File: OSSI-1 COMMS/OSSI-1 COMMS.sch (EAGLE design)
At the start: 188 parts, among them Q1 NX-3215, U1 MAX2640, U10 MAX6369, U11 TPS3838, U12 MAX890L, U13 MCP1700_SOT23, U2 PE4259, U3 RF5110G, U4 OPA347, U5 MAX869L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

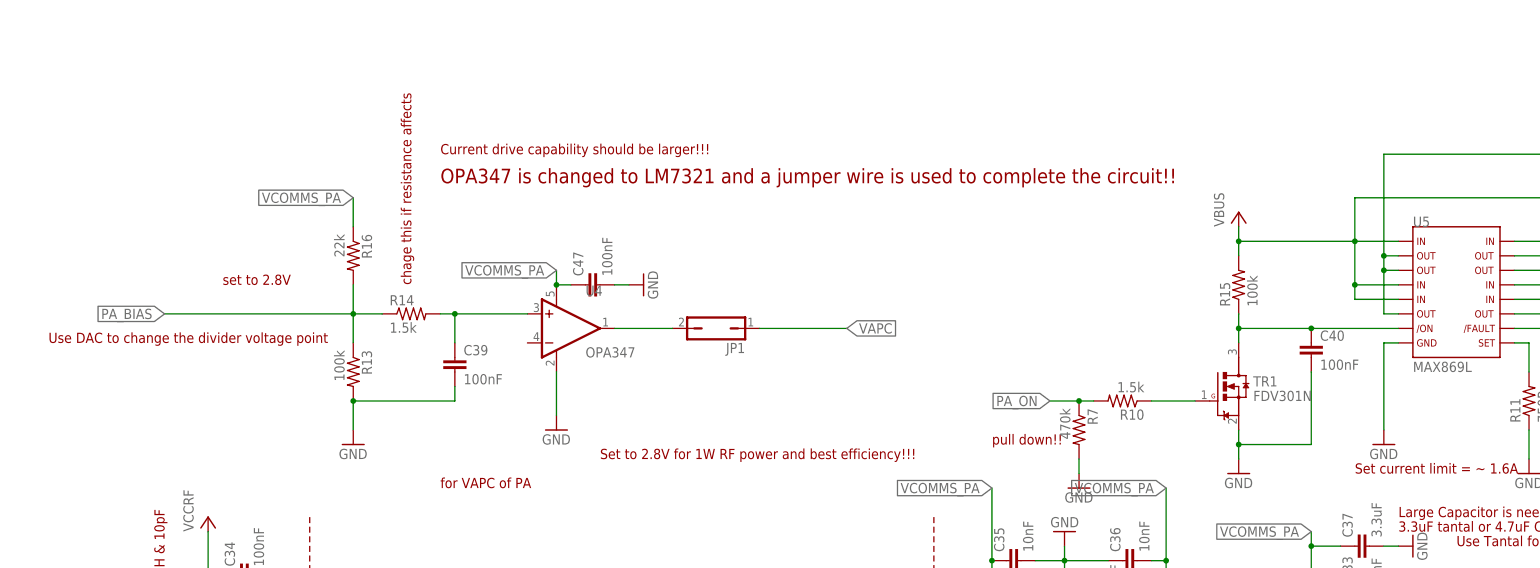
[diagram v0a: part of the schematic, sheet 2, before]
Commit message: opa347 setting corrected
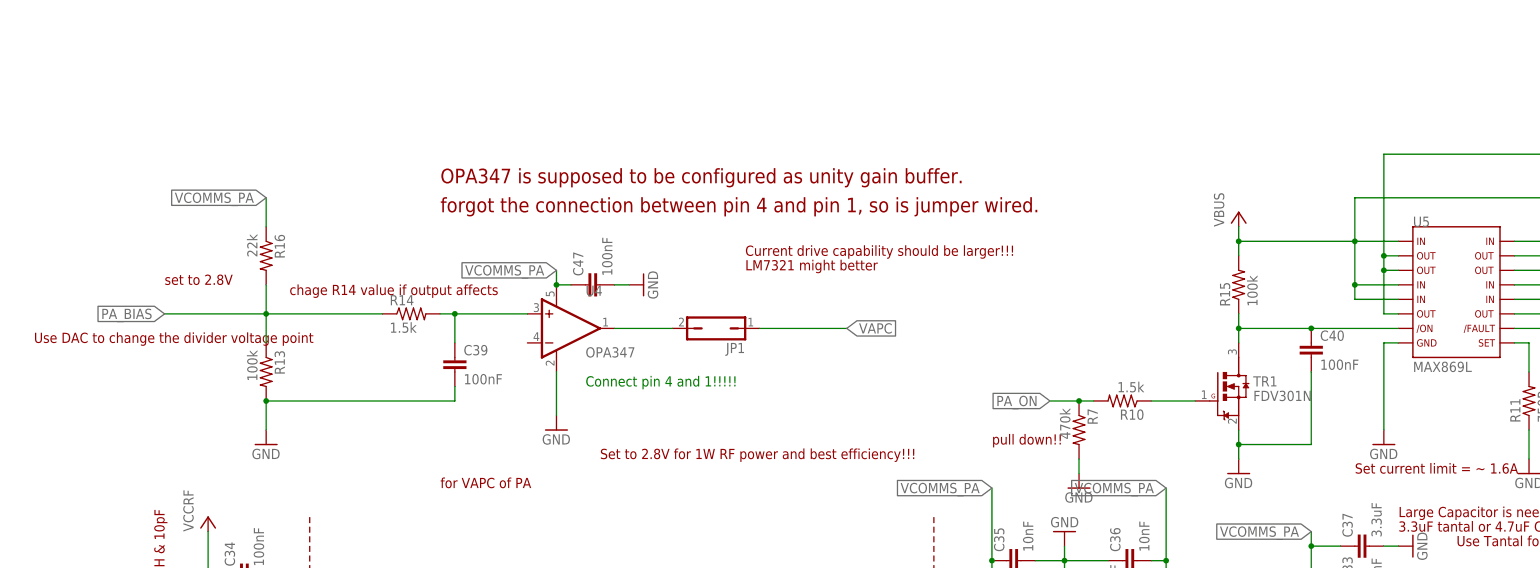
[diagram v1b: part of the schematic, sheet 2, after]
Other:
- note added: "Connect pin 4 and 1!!!!!"
- note added: "LM7321 might better"
- note added: "OPA347 is supposed to be configured as unity gain buffer."
- note added: "chage R14 value if output affects"
- note added: "forgot the connection between pin 4 and pin 1, so is jumper wired."
- note removed: "OPA347 is changed to LM7321 and a jumper wire is used to complete the circuit!!"
- note removed: "chage this if resistance affects"
- moved on the sheet: R13, R16
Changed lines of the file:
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@@
 <text x="269.24" y="55.88" size="1.778" layer="94">post impedance matching</text>
 <text x="78.74" y="200.66" size="1.778" layer="94">for VAPC of PA </text>
-<text x="40.64" y="236.22" size="1.778" layer="94">set to 2.8V</text>
-<text x="10.16" y="226.06" size="1.778" layer="94">Use DAC to change the divider voltage point</text>
+<text x="30.48" y="236.22" size="1.778" layer="94">set to 2.8V</text>
+<text x="7.62" y="226.06" size="1.778" layer="94">Use DAC to change the divider voltage point</text>
 <text x="27.94" y="147.32" size="1.778" layer="94">0dbm </text>
 <text x="292.1" y="162.56" size="1.778" layer="94">1Watt </text>
@@
 <text x="241.3" y="160.02" size="1.778" layer="94">important!!</text>
 <text x="233.68" y="165.1" size="1.778" layer="94">important!!</text>
-<text x="73.66" y="236.22" size="1.778" layer="94" rot="R90">chage this if resistance affects</text>
+<text x="88.9" y="236.22" size="1.778" layer="94" rot="R180">chage R14 value if output affects</text>
 <text x="175.26" y="208.28" size="1.778" layer="94">pull down!!</text>
 <wire x1="111.76" y1="91.44" x2="111.76" y2="25.4" width="0.1524" layer="94" style="shortdash"/>
@@
 <text x="30.48" y="160.02" size="1.778" layer="94" rot="R90">Eval board settng is 13nH &amp; 10pF</text>
 <text x="322.58" y="190.5" size="1.778" layer="94">Set VCOMMS_PA to 3.3~3.4V</text>
-<text x="78.74" y="259.08" size="1.778" layer="94">Current drive capability should be larger!!!</text>
-<text x="78.74" y="254" size="2.54" layer="94">OPA347 is changed to LM7321 and a jumper wire is used to complete the circuit!!</text>
+<text x="132.08" y="241.3" size="1.778" layer="94">Current drive capability should be larger!!!</text>
+<text x="78.74" y="254" size="2.54" layer="94">OPA347 is supposed to be configured as unity gain buffer.</text>
 <text x="106.68" y="205.74" size="1.778" layer="94">Set to 2.8V for 1W RF power and best efficiency!!!</text>
 <text x="200.66" y="93.98" size="1.778" layer="94">Use Tantal for larger RF out</text>
@@
 <text x="289.56" y="27.94" size="3.302" layer="94" font="vector">OPEN SOURSE SATELLITE INITIATIVE</text>
 <text x="289.56" y="25.4" size="2.54" layer="94" font="vector">http://opensat.cc</text>
+<text x="78.74" y="248.92" size="2.54" layer="94">forgot the connection between pin 4 and pin 1, so is jumper wired.</text>
+<text x="104.14" y="218.44" size="1.778" layer="91">Connect pin 4 and 1!!!!!</text>
+<text x="132.08" y="238.76" size="1.778" layer="94">LM7321 might better</text>
 </plain>
 <instances>
@@
 <instance part="VCCRF3" gate="G$1" x="38.1" y="195.58"/>
 <instance part="VCCRF4" gate="G$1" x="129.54" y="81.28"/>
-<instance part="R16" gate="G$1" x="63.5" y="241.3" rot="R270"/>
-<instance part="R13" gate="G$1" x="63.5" y="220.98" rot="R270"/>
+<instance part="R16" gate="G$1" x="48.26" y="241.3" rot="R270"/>
+<instance part="R13" gate="G$1" x="48.26" y="220.98" rot="R270"/>
 <instance part="C39" gate="G$1" x="81.28" y="223.52"/>
-<instance part="GND63" gate="1" x="63.5" y="208.28"/>
+<instance part="GND63" gate="1" x="48.26" y="208.28"/>
 <instance part="GND64" gate="1" x="99.06" y="210.82"/>
 <instance part="U4" gate="A" x="101.6" y="228.6"/>
@@
 <pinref part="GND63" gate="1" pin="GND"/>
 <pinref part="R13" gate="G$1" pin="2"/>
-<wire x1="63.5" y1="210.82" x2="63.5" y2="215.9" width="0.1524" layer="91"/>
+<wire x1="48.26" y1="210.82" x2="48.26" y2="215.9" width="0.1524" layer="91"/>
 <pinref part="C39" gate="G$1" pin="2"/>
 <wire x1="81.28" y1="218.44" x2="81.28" y2="215.9" width="0.1524" layer="91"/>
-<wire x1="81.28" y1="215.9" x2="63.5" y2="215.9" width="0.1524" layer="91"/>
-<junction x="63.5" y="215.9"/>
+<wire x1="81.28" y1="215.9" x2="48.26" y2="215.9" width="0.1524" layer="91"/>
+<junction x="48.26" y="215.9"/>
 </segment>
 <segment>
@@
 <segment>
 <pinref part="R16" gate="G$1" pin="1"/>
-<wire x1="63.5" y1="246.38" x2="63.5" y2="251.46" width="0.1524" layer="91"/>
-<label x="63.5" y="251.46" size="1.778" layer="95" rot="R180" xref="yes"/>
+<wire x1="48.26" y1="246.38" x2="48.26" y2="251.46" width="0.1524" layer="91"/>
+<label x="48.26" y="251.46" size="1.778" layer="95" rot="R180" xref="yes"/>
 </segment>
 <segment>
@@
 <segment>
 <pinref part="R16" gate="G$1" pin="2"/>
-<wire x1="63.5" y1="231.14" x2="63.5" y2="236.22" width="0.1524" layer="91"/>
+<wire x1="48.26" y1="231.14" x2="48.26" y2="236.22" width="0.1524" layer="91"/>
 <pinref part="R13" gate="G$1" pin="1"/>
-<wire x1="63.5" y1="231.14" x2="63.5" y2="226.06" width="0.1524" layer="91"/>
-<junction x="63.5" y="231.14"/>
-<wire x1="63.5" y1="231.14" x2="30.48" y2="231.14" width="0.1524" layer="91"/>
+<wire x1="48.26" y1="231.14" x2="48.26" y2="226.06" width="0.1524" layer="91"/>
+<junction x="48.26" y="231.14"/>
+<wire x1="48.26" y1="231.14" x2="30.48" y2="231.14" width="0.1524" layer="91"/>
 <label x="30.48" y="231.14" size="1.778" layer="95" rot="R180" xref="yes"/>
 <pinref part="R14" gate="G$1" pin="1"/>
-<wire x1="63.5" y1="231.14" x2="68.58" y2="231.14" width="0.1524" layer="91"/>
-</segment>
-</net>
+<wire x1="48.26" y1="231.14" x2="68.58" y2="231.14" width="0.1524" layer="91"/>
+</segment>
+</net>

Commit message: sch corrected
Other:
- note added: "15pF"
- note removed: "8.2nH"
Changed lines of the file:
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@@
 <text x="223.52" y="121.92" size="1.778" layer="94">10pF +6pF  is better than 16 pF why???</text>
 <text x="299.72" y="116.84" size="1.778" layer="94">tune RF switch to lower the insertion loss. currently around 1.2 dB loss!!!!</text>
-<text x="193.04" y="50.8" size="1.778" layer="91">1500pF</text>
-<text x="180.34" y="50.8" size="1.778" layer="91">47nH</text>
-<text x="116.84" y="45.72" size="1.778" layer="91">8.2nH</text>
+<text x="193.04" y="45.72" size="1.778" layer="91">1500pF</text>
+<text x="180.34" y="45.72" size="1.778" layer="91">47nH</text>
+<text x="116.84" y="45.72" size="1.778" layer="91">15pF</text>
 <text x="116.84" y="43.18" size="1.778" layer="91">Final Value but the result will be similar</text>
 <text x="48.26" y="66.04" size="1.778" layer="91">12pF</text>

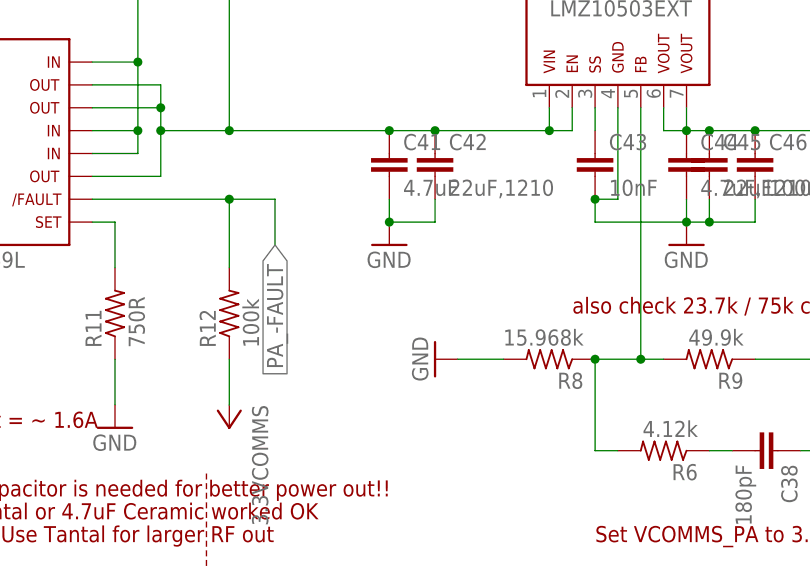
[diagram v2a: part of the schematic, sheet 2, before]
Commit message: value comment changed
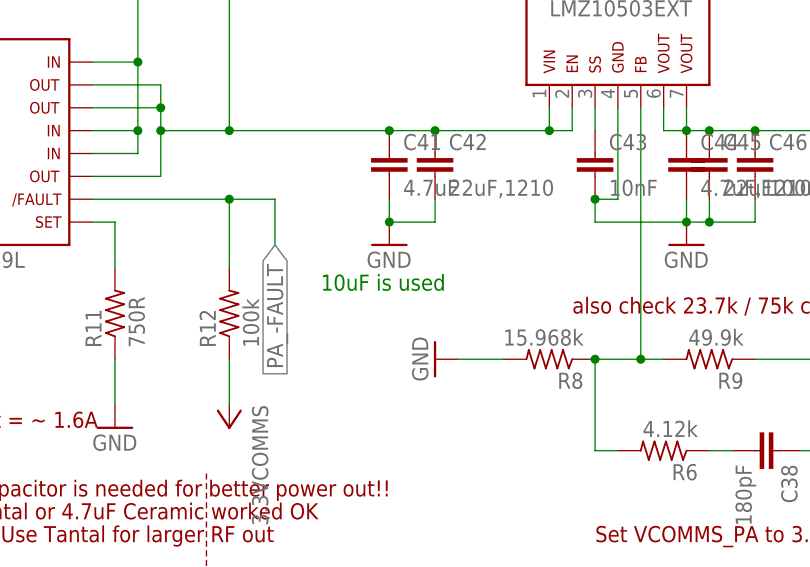
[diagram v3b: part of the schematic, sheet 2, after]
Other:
- note added: "10uF is used"
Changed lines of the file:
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@@
 <text x="104.14" y="218.44" size="1.778" layer="91">Connect pin 4 and 1!!!!!</text>
 <text x="132.08" y="238.76" size="1.778" layer="94">LM7321 might better</text>
+<text x="292.1" y="218.44" size="1.778" layer="91">10uF is used</text>
 </plain>
 <instances>

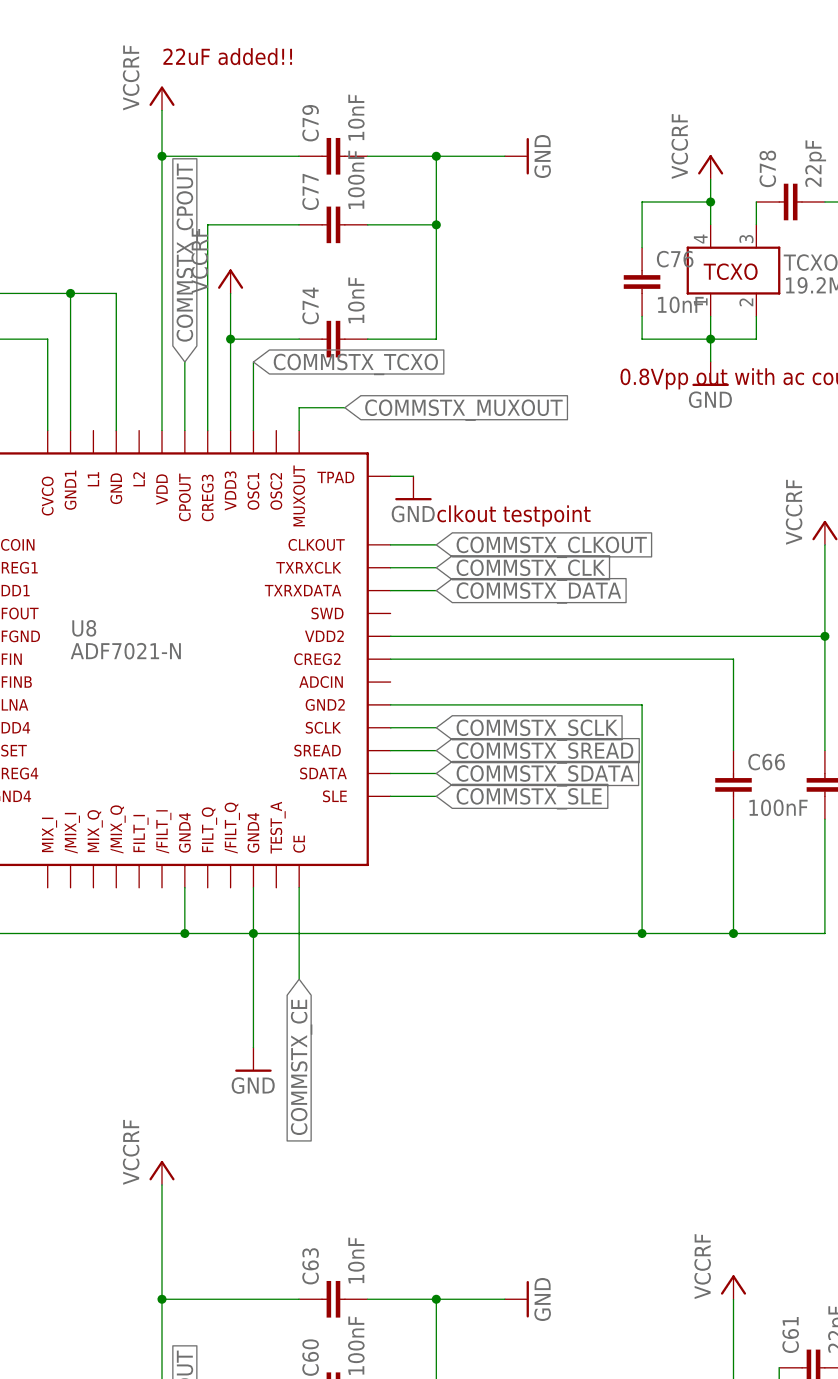
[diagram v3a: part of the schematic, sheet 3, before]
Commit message: tuning power cap commet added
22uF near the adf7021-n is added for better performance by lowering the
power noised
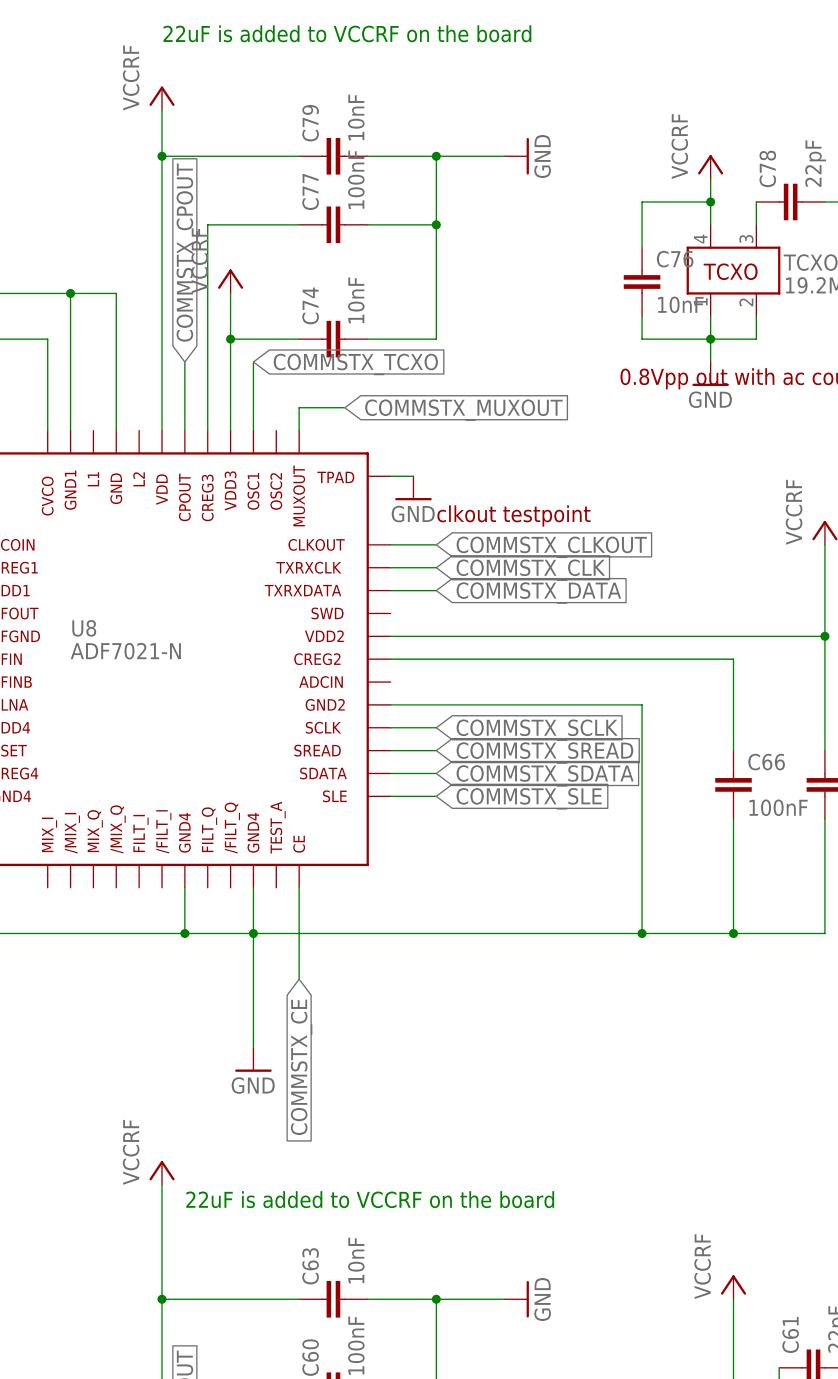
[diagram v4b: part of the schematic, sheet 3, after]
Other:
- note added: "22uF is added to VCCRF on the board"
- note removed: "22uF added!!"
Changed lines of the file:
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@@
 <text x="243.84" y="88.9" size="1.778" layer="94">0.8Vpp out with ac coupled capacitor</text>
 <text x="243.84" y="223.52" size="1.778" layer="94">0.8Vpp out with ac coupled capacitor</text>
-<text x="193.04" y="259.08" size="1.778" layer="94">22uF added!!</text>
 <text x="68.58" y="243.84" size="1.778" layer="94">110 is used</text>
 <text x="71.12" y="127" size="1.778" layer="94">110 is used</text>
 <text x="289.56" y="27.94" size="3.302" layer="94" font="vector">OPEN SOURSE SATELLITE INITIATIVE</text>
 <text x="289.56" y="25.4" size="2.54" layer="94" font="vector">http://opensat.cc</text>
+<text x="193.04" y="261.62" size="1.778" layer="91">22uF is added to VCCRF on the board </text>
+<text x="195.58" y="132.08" size="1.778" layer="91">22uF is added to VCCRF on the board </text>
 </plain>
 <instances>
